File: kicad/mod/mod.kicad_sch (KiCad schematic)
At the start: 7 parts, among them J1 In, J2 Out, J3 Program Pins, U1 AP7384-33SA, U2 ATtiny402-SS

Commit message: Meh
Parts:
- added C2: 100nF, Capacitor_SMD:C_0805_2012Metric, symbol Device:C
- added C3: 1µF, Capacitor_SMD:C_0805_2012Metric, symbol Device:C
- C1, R1: footprint (none) -> Capacitor_SMD:C_0805_2012Metric
- J1, J2: footprint (none) -> Connector_PinHeader_2.00mm:PinHeader_2x03_P2.00mm_Vertical
- J3: footprint (none) -> Connector_PinHeader_2.54mm:PinHeader_1x03_P2.54mm_Vertical
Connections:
- net +12V: now also J1.5 (Pin_5), C3.1; no longer J1.1 (Pin_1)
- net GND: now also J1.1 (Pin_1), J1.2 (Pin_2), C2.1, C3.2; no longer J1.5 (Pin_5), J1.6 (Pin_6)
- net at C1.1, U1.2 (VO), U2.1 (VCC): now also C2.2
- no-connect marks 3 -> 5
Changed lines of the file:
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@@
     (rev "1")
   )
+  (junction (at 40.64 35.56) (diameter 0.9144) (color 0 0 0 0))
   (junction (at 55.88 40.64) (diameter 0.9144) (color 0 0 0 0))
   (junction (at 58.42 35.56) (diameter 0.9144) (color 0 0 0 0))
   (junction (at 71.12 35.56) (diameter 0.9144) (color 0 0 0 0))
+  (junction (at 71.12 73.66) (diameter 0.9144) (color 0 0 0 0))
   (junction (at 99.06 73.66) (diameter 0.9144) (color 0 0 0 0))
+  (junction (at 121.92 83.82) (diameter 0.9144) (color 0 0 0 0))
+  (junction (at 121.92 116.84) (diameter 0.9144) (color 0 0 0 0))
   (junction (at 142.24 60.96) (diameter 0.9144) (color 0 0 0 0))
   (no_connect (at 71.12 40.64))
+  (no_connect (at 104.14 35.56))
+  (no_connect (at 104.14 38.1))
   (no_connect (at 104.14 40.64))
   (no_connect (at 137.16 106.68))
@@
     (stroke (width 0) (type solid) (color 0 0 0 0))
   )
-  (wire (pts (xy 121.92 73.66) (xy 121.92 86.36))
+  (wire (pts (xy 99.06 90.17) (xy 99.06 96.52))
+    (stroke (width 0) (type solid) (color 0 0 0 0))
+  )
+  (wire (pts (xy 99.06 90.17) (xy 107.95 90.17))
+    (stroke (width 0) (type solid) (color 0 0 0 0))
+  )
+  (wire (pts (xy 99.06 116.84) (xy 99.06 104.14))
+    (stroke (width 0) (type solid) (color 0 0 0 0))
+  )
+  (wire (pts (xy 99.06 116.84) (xy 121.92 116.84))
+    (stroke (width 0) (type solid) (color 0 0 0 0))
+  )
+  (wire (pts (xy 107.95 83.82) (xy 121.92 83.82))
+    (stroke (width 0) (type solid) (color 0 0 0 0))
+  )
+  (wire (pts (xy 107.95 90.17) (xy 107.95 83.82))
+    (stroke (width 0) (type solid) (color 0 0 0 0))
+  )
+  (wire (pts (xy 121.92 73.66) (xy 121.92 83.82))
+    (stroke (width 0) (type solid) (color 0 0 0 0))
+  )
+  (wire (pts (xy 121.92 83.82) (xy 121.92 86.36))
     (stroke (width 0) (type solid) (color 0 0 0 0))
   )
@@
     (effects (font (size 1.27 1.27)) (justify right bottom))
   )
+  (symbol (lib_id "power:PWR_FLAG") (at 40.64 35.56 90) (unit 1)
+    (in_bom yes) (on_board yes)
+    (property "Reference" "#FLG0101" (id 0) (at 38.735 35.56 0)
+      (effects (font (size 1.27 1.27)) hide)
+    )
+    (property "Value" "PWR_FLAG" (id 1) (at 36.83 35.56 90)
+      (effects (font (size 1.27 1.27)) (justify left))
+    )
+    (property "Footprint" "" (id 2) (at 40.64 35.56 0)
+      (effects (font (size 1.27 1.27)) hide)
+    )
+    (property "Datasheet" "~" (id 3) (at 40.64 35.56 0)
+      (effects (font (size 1.27 1.27)) hide)
+    )
+    (pin "1")
+  )
   (symbol (lib_id "power:PWR_FLAG") (at 55.88 40.64 90) (unit 1)
     (in_bom yes) (on_board yes)
@@
     (pin "1")
   )
+  (symbol (lib_id "power:GND") (at 71.12 81.28 0) (unit 1)
+    (in_bom yes) (on_board yes)
+    (property "Reference" "#PWR0102" (id 0) (at 71.12 87.63 0)
+      (effects (font (size 1.27 1.27)) hide)
+    )
+    (property "Value" "GND" (id 1) (at 72.39 86.36 0))
+    (property "Footprint" "" (id 2) (at 71.12 81.28 0)
+      (effects (font (size 1.27 1.27)) hide)
+    )
+    (property "Datasheet" "" (id 3) (at 71.12 81.28 0)
+      (effects (font (size 1.27 1.27)) hide)
+    )
+    (pin "1")
+  )
   (symbol (lib_id "power:GND") (at 81.28 35.56 270) (unit 1)
     (in_bom yes) (on_board yes)
@@
   (symbol (lib_id "power:GND") (at 132.08 60.96 0) (unit 1)
     (in_bom yes) (on_board yes)
-    (property "Reference" "#PWR?" (id 0) (at 132.08 67.31 0)
+    (property "Reference" "#PWR0101" (id 0) (at 132.08 67.31 0)
       (effects (font (size 1.27 1.27)) hide)
     )
@@
       (effects (font (size 1.27 1.27)) (justify left))
     )
-    (property "Footprint" "" (id 2) (at 140.462 57.15 90)
+    (property "Footprint" "Capacitor_SMD:C_0805_2012Metric" (id 2) (at 140.462 57.15 90)
       (effects (font (size 1.27 1.27)) hide)
     )
@@
     (pin "2")
   )
+  (symbol (lib_id "Device:C") (at 71.12 77.47 0) (unit 1)
+    (in_bom yes) (on_board yes)
+    (property "Reference" "C3" (id 0) (at 74.93 76.2 0)
+      (effects (font (size 1.27 1.27)) (justify left))
+    )
+    (property "Value" "1µF" (id 1) (at 74.93 78.74 0)
+      (effects (font (size 1.27 1.27)) (justify left))
+    )
+    (property "Footprint" "Capacitor_SMD:C_0805_2012Metric" (id 2) (at 72.0852 81.28 0)
+      (effects (font (size 1.27 1.27)) hide)
+    )
+    (property "Datasheet" "~" (id 3) (at 71.12 77.47 0)
+      (effects (font (size 1.27 1.27)) hide)
+    )
+    (pin "1")
+    (pin "2")
+  )
   (symbol (lib_id "Device:C") (at 99.06 77.47 0) (unit 1)
     (in_bom yes) (on_board yes)
@@
       (effects (font (size 1.27 1.27)) (justify left))
     )
-    (property "Footprint" "" (id 2) (at 100.0252 81.28 0)
+    (property "Footprint" "Capacitor_SMD:C_0805_2012Metric" (id 2) (at 100.0252 81.28 0)
       (effects (font (size 1.27 1.27)) hide)
     )
     (property "Datasheet" "~" (id 3) (at 99.06 77.47 0)
+      (effects (font (size 1.27 1.27)) hide)
+    )
+    (pin "1")
+    (pin "2")
+  )
+  (symbol (lib_id "Device:C") (at 99.06 100.33 180) (unit 1)
+    (in_bom yes) (on_board yes)
+    (property "Reference" "C2" (id 0) (at 102.87 99.06 0)
+      (effects (font (size 1.27 1.27)) (justify right))
+    )
+    (property "Value" "100nF" (id 1) (at 102.87 101.6 0)
+      (effects (font (size 1.27 1.27)) (justify right))
+    )
+    (property "Footprint" "Capacitor_SMD:C_0805_2012Metric" (id 2) (at 98.0948 96.52 0)
+      (effects (font (size 1.27 1.27)) hide)
+    )
+    (property "Datasheet" "~" (id 3) (at 99.06 100.33 0)
       (effects (font (size 1.27 1.27)) hide)
     )
@@
     (property "Reference" "J3" (id 0) (at 128.27 48.26 0))
     (property "Value" "Program Pins" (id 1) (at 128.27 50.8 0))
-    (property "Footprint" "" (id 2) (at 124.46 55.88 0)
+    (property "Footprint" "Connector_PinHeader_2.54mm:PinHeader_1x03_P2.54mm_Vertical" (id 2) (at 124.46 55.88 0)
       (effects (font (size 1.27 1.27)) hide)
     )
@@
     (pin "3")
   )
-  (symbol (lib_id "Connector_Generic:Conn_02x03_Odd_Even") (at 63.5 38.1 0) (mirror x) (unit 1)
-    (in_bom yes) (on_board yes)
-    (property "Reference" "J1" (id 0) (at 64.77 29.21 0))
-    (property "Value" "In" (id 1) (at 64.77 31.75 0))
-    (property "Footprint" "" (id 2) (at 63.5 38.1 0)
+  (symbol (lib_id "Connector_Generic:Conn_02x03_Odd_Even") (at 63.5 38.1 0) (unit 1)
+    (in_bom yes) (on_board yes)
+    (property "Reference" "J1" (id 0) (at 64.77 31.75 0))
+    (property "Value" "In" (id 1) (at 64.77 29.21 0))
+    (property "Footprint" "Connector_PinHeader_2.00mm:PinHeader_2x03_P2.00mm_Vertical" (id 2) (at 63.5 38.1 0)
       (effects (font (size 1.27 1.27)) hide)
     )
@@
     (property "Reference" "J2" (id 0) (at 97.79 29.21 0))
     (property "Value" "Out" (id 1) (at 97.79 31.75 0))
-    (property "Footprint" "" (id 2) (at 96.52 38.1 0)
+    (property "Footprint" "Connector_PinHeader_2.00mm:PinHeader_2x03_P2.00mm_Vertical" (id 2) (at 96.52 38.1 0)
       (effects (font (size 1.27 1.27)) hide)
     )
@@
   (symbol (lib_id "MCU_Microchip_ATtiny:ATtiny402-SS") (at 121.92 101.6 0) (unit 1)
     (in_bom yes) (on_board yes)
-    (property "Reference" "U2" (id 0) (at 107.95 100.33 0)
+    (property "Reference" "U2" (id 0) (at 121.92 101.6 0)
       (effects (font (size 1.27 1.27)) (justify right))
     )
-    (property "Value" "ATtiny402-SS" (id 1) (at 107.95 102.87 0)
+    (property "Value" "ATtiny402-SS" (id 1) (at 127 106.68 0)
       (effects (font (size 1.27 1.27)) (justify right))
     )
@@
       (reference "#FLG01") (unit 1) (value "PWR_FLAG") (footprint "")
     )
+    (path "/928e5337-613b-4307-8298-b337ca15fc47"
+      (reference "#FLG0101") (unit 1) (value "PWR_FLAG") (footprint "")
+    )
     (path "/e33dedd4-4100-43ea-9038-ea912e5a8d37"
       (reference "#PWR01") (unit 1) (value "GND") (footprint "")
@@
     )
     (path "/ae38171d-9150-4ae7-bb5e-7b15d486b2b1"
-      (reference "#PWR?") (unit 1) (value "GND") (footprint "")
+      (reference "#PWR0101") (unit 1) (value "GND") (footprint "")
+    )
+    (path "/0bc015a7-0a9a-4ba5-9c66-6b46aefe101a"
+      (reference "#PWR0102") (unit 1) (value "GND") (footprint "")
     )
     (path "/f10cebee-5712-4587-b3e7-0045452f1d20"
-      (reference "C1") (unit 1) (value "1µF") (footprint "")
+      (reference "C1") (unit 1) (value "1µF") (footprint "Capacitor_SMD:C_0805_2012Metric")
+    )
+    (path "/81357930-264e-4e0e-9cf7-2accc43945d8"
+      (reference "C2") (unit 1) (value "100nF") (footprint "Capacitor_SMD:C_0805_2012Metric")
+    )
+    (path "/44c455e1-9bcb-4a33-bad2-ca8a2d34a438"
+      (reference "C3") (unit 1) (value "1µF") (footprint "Capacitor_SMD:C_0805_2012Metric")
     )
     (path "/72fa8a6a-1001-4fc7-ab89-fc778a9ae985"
-      (reference "J1") (unit 1) (value "In") (footprint "")
+      (reference "J1") (unit 1) (value "In") (footprint "Connector_PinHeader_2.00mm:PinHeader_2x03_P2.00mm_Vertical")
     )
     (path "/e9954cfa-616e-4b19-8bda-17822bdd089e"
-      (reference "J2") (unit 1) (value "Out") (footprint "")
+      (reference "J2") (unit 1) (value "Out") (footprint "Connector_PinHeader_2.00mm:PinHeader_2x03_P2.00mm_Vertical")
     )
     (path "/c25d2fd2-3751-4f59-bba4-51cd807d3f08"
-      (reference "J3") (unit 1) (value "Program Pins") (footprint "")
+      (reference "J3") (unit 1) (value "Program Pins") (footprint "Connector_PinHeader_2.54mm:PinHeader_1x03_P2.54mm_Vertical")
     )
     (path "/8faf5ccf-9a82-42b1-9ba4-1ce9f91db140"
-      (reference "R1") (unit 1) (value "4K7") (footprint "")
+      (reference "R1") (unit 1) (value "4K7") (footprint "Capacitor_SMD:C_0805_2012Metric")
     )
     (path "/76f352f7-450b-4ad2-8e0a-6bb76cd96f63"

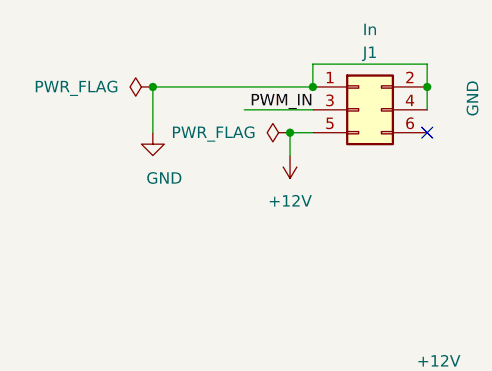
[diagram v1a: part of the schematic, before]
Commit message: Started layout
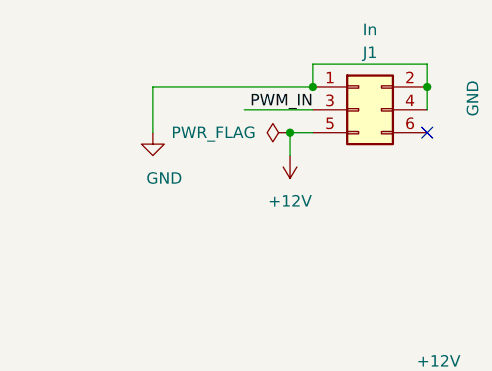
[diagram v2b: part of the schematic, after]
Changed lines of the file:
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@@
     (rev "1")
   )
-  (junction (at 40.64 35.56) (diameter 0.9144) (color 0 0 0 0))
   (junction (at 55.88 40.64) (diameter 0.9144) (color 0 0 0 0))
   (junction (at 58.42 35.56) (diameter 0.9144) (color 0 0 0 0))
@@
     (effects (font (size 1.27 1.27)) (justify right bottom))
   )
-  (symbol (lib_id "power:PWR_FLAG") (at 40.64 35.56 90) (unit 1)
-    (in_bom yes) (on_board yes)
-    (property "Reference" "#FLG0101" (id 0) (at 38.735 35.56 0)
-      (effects (font (size 1.27 1.27)) hide)
-    )
-    (property "Value" "PWR_FLAG" (id 1) (at 36.83 35.56 90)
-      (effects (font (size 1.27 1.27)) (justify left))
-    )
-    (property "Footprint" "" (id 2) (at 40.64 35.56 0)
-      (effects (font (size 1.27 1.27)) hide)
-    )
-    (property "Datasheet" "~" (id 3) (at 40.64 35.56 0)
-      (effects (font (size 1.27 1.27)) hide)
-    )
-    (pin "1")
-  )
   (symbol (lib_id "power:PWR_FLAG") (at 55.88 40.64 90) (unit 1)
     (in_bom yes) (on_board yes)
@@
       (reference "#FLG01") (unit 1) (value "PWR_FLAG") (footprint "")
     )
-    (path "/928e5337-613b-4307-8298-b337ca15fc47"
-      (reference "#FLG0101") (unit 1) (value "PWR_FLAG") (footprint "")
-    )
     (path "/e33dedd4-4100-43ea-9038-ea912e5a8d37"

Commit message: Meh 2
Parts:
- added J4, J5: I2C, Connector_PinHeader_2.54mm:PinHeader_1x03_P2.54mm_Vertical, symbol Connector:Conn_01x03_Male
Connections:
- net GND: now also J4.3 (Pin_3), J5.3 (Pin_3)
- net SCL: now also J4.2 (Pin_2), J5.2 (Pin_2)
- net SDA: now also J4.1 (Pin_1), J5.1 (Pin_1)
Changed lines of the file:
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@@
   (junction (at 121.92 116.84) (diameter 0.9144) (color 0 0 0 0))
   (junction (at 142.24 60.96) (diameter 0.9144) (color 0 0 0 0))
+  (junction (at 149.86 96.52) (diameter 0.9144) (color 0 0 0 0))
+  (junction (at 152.4 99.06) (diameter 0.9144) (color 0 0 0 0))
+  (junction (at 154.94 101.6) (diameter 0.9144) (color 0 0 0 0))
   (no_connect (at 71.12 40.64))
   (no_connect (at 104.14 35.56))
@@
     (stroke (width 0) (type solid) (color 0 0 0 0))
   )
-  (wire (pts (xy 137.16 96.52) (xy 147.32 96.52))
-    (stroke (width 0) (type solid) (color 0 0 0 0))
-  )
-  (wire (pts (xy 137.16 99.06) (xy 147.32 99.06))
+  (wire (pts (xy 137.16 96.52) (xy 149.86 96.52))
+    (stroke (width 0) (type solid) (color 0 0 0 0))
+  )
+  (wire (pts (xy 137.16 99.06) (xy 152.4 99.06))
     (stroke (width 0) (type solid) (color 0 0 0 0))
   )
@@
   )
   (wire (pts (xy 142.24 93.98) (xy 137.16 93.98))
+    (stroke (width 0) (type solid) (color 0 0 0 0))
+  )
+  (wire (pts (xy 149.86 83.82) (xy 156.21 83.82))
+    (stroke (width 0) (type solid) (color 0 0 0 0))
+  )
+  (wire (pts (xy 149.86 96.52) (xy 149.86 83.82))
+    (stroke (width 0) (type solid) (color 0 0 0 0))
+  )
+  (wire (pts (xy 149.86 96.52) (xy 156.21 96.52))
+    (stroke (width 0) (type solid) (color 0 0 0 0))
+  )
+  (wire (pts (xy 152.4 86.36) (xy 156.21 86.36))
+    (stroke (width 0) (type solid) (color 0 0 0 0))
+  )
+  (wire (pts (xy 152.4 99.06) (xy 152.4 86.36))
+    (stroke (width 0) (type solid) (color 0 0 0 0))
+  )
+  (wire (pts (xy 152.4 99.06) (xy 156.21 99.06))
+    (stroke (width 0) (type solid) (color 0 0 0 0))
+  )
+  (wire (pts (xy 152.4 101.6) (xy 152.4 116.84))
+    (stroke (width 0) (type solid) (color 0 0 0 0))
+  )
+  (wire (pts (xy 152.4 116.84) (xy 121.92 116.84))
+    (stroke (width 0) (type solid) (color 0 0 0 0))
+  )
+  (wire (pts (xy 154.94 88.9) (xy 156.21 88.9))
+    (stroke (width 0) (type solid) (color 0 0 0 0))
+  )
+  (wire (pts (xy 154.94 101.6) (xy 152.4 101.6))
+    (stroke (width 0) (type solid) (color 0 0 0 0))
+  )
+  (wire (pts (xy 154.94 101.6) (xy 154.94 88.9))
+    (stroke (width 0) (type solid) (color 0 0 0 0))
+  )
+  (wire (pts (xy 156.21 101.6) (xy 154.94 101.6))
     (stroke (width 0) (type solid) (color 0 0 0 0))
   )
@@
     )
     (property "Datasheet" "~" (id 3) (at 124.46 55.88 0)
+      (effects (font (size 1.27 1.27)) hide)
+    )
+    (pin "1")
+    (pin "2")
+    (pin "3")
+  )
+  (symbol (lib_id "Connector:Conn_01x03_Male") (at 161.29 86.36 0) (mirror y) (unit 1)
+    (in_bom yes) (on_board yes)
+    (property "Reference" "J5" (id 0) (at 157.48 78.74 0))
+    (property "Value" "I2C" (id 1) (at 157.48 81.28 0))
+    (property "Footprint" "Connector_PinHeader_2.54mm:PinHeader_1x03_P2.54mm_Vertical" (id 2) (at 161.29 86.36 0)
+      (effects (font (size 1.27 1.27)) hide)
+    )
+    (property "Datasheet" "~" (id 3) (at 161.29 86.36 0)
+      (effects (font (size 1.27 1.27)) hide)
+    )
+    (pin "1")
+    (pin "2")
+    (pin "3")
+  )
+  (symbol (lib_id "Connector:Conn_01x03_Male") (at 161.29 99.06 0) (mirror y) (unit 1)
+    (in_bom yes) (on_board yes)
+    (property "Reference" "J4" (id 0) (at 157.48 91.44 0))
+    (property "Value" "I2C" (id 1) (at 157.48 93.98 0))
+    (property "Footprint" "Connector_PinHeader_2.54mm:PinHeader_1x03_P2.54mm_Vertical" (id 2) (at 161.29 99.06 0)
+      (effects (font (size 1.27 1.27)) hide)
+    )
+    (property "Datasheet" "~" (id 3) (at 161.29 99.06 0)
       (effects (font (size 1.27 1.27)) hide)
     )
@@
       (reference "J3") (unit 1) (value "Program Pins") (footprint "Connector_PinHeader_2.54mm:PinHeader_1x03_P2.54mm_Vertical")
     )
+    (path "/51eda64b-bb75-40a2-bbc2-1868dfa70b79"
+      (reference "J4") (unit 1) (value "I2C") (footprint "Connector_PinHeader_2.54mm:PinHeader_1x03_P2.54mm_Vertical")
+    )
+    (path "/b5e0e696-444a-4199-9ca6-a6dcb96416da"
+      (reference "J5") (unit 1) (value "I2C") (footprint "Connector_PinHeader_2.54mm:PinHeader_1x03_P2.54mm_Vertical")
+    )
     (path "/8faf5ccf-9a82-42b1-9ba4-1ce9f91db140"
